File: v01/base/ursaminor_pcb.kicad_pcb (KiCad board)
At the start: 2 copper layers, 298.8 x 122 mm, 143 parts, among them J1 USB_C_Receptacle_USB2.0, J2 I2C-L, J3 I2C-R, J4 AVR-ISP-6, SW1 Reset, U1 ATmega32U4-AU, U2 MCP23017_SO, U3 PRTR5V0U2X, U4 HOLE, Y1 16Mhz

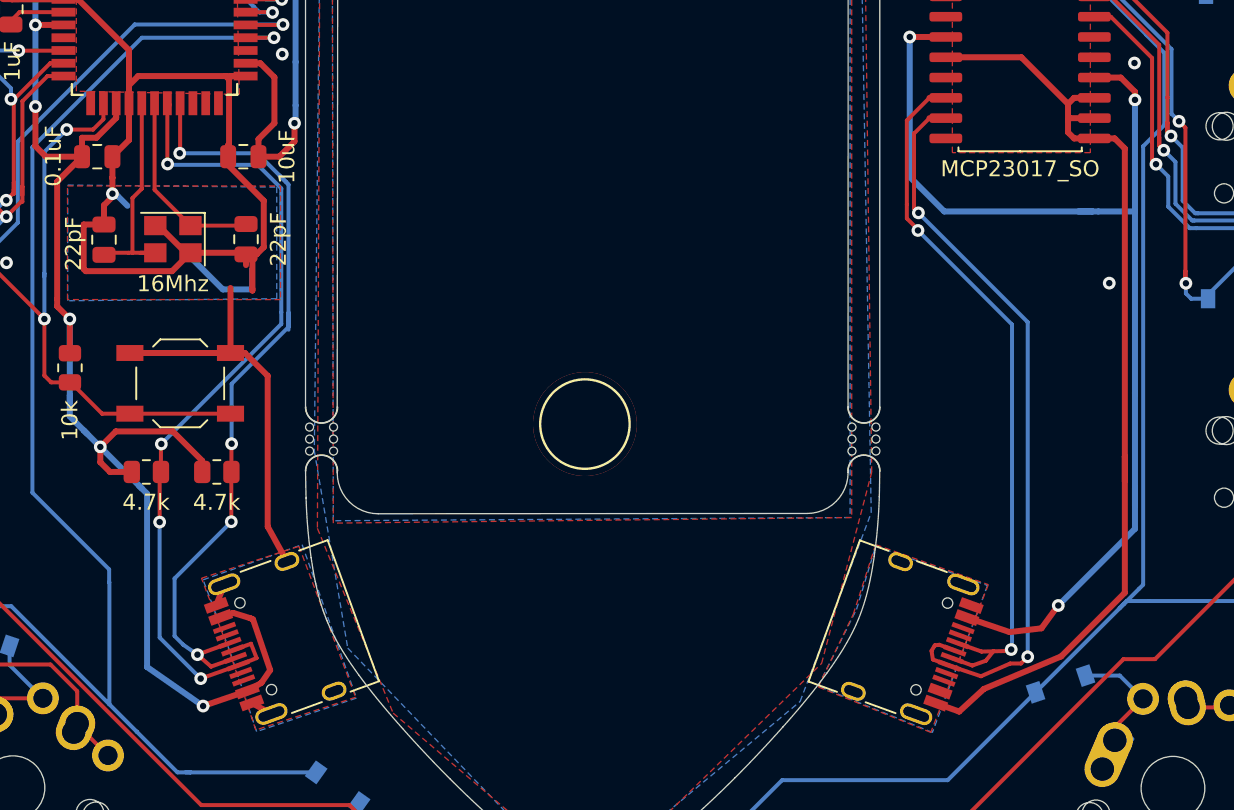
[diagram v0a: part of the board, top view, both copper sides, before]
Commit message: Rename files and update path references.
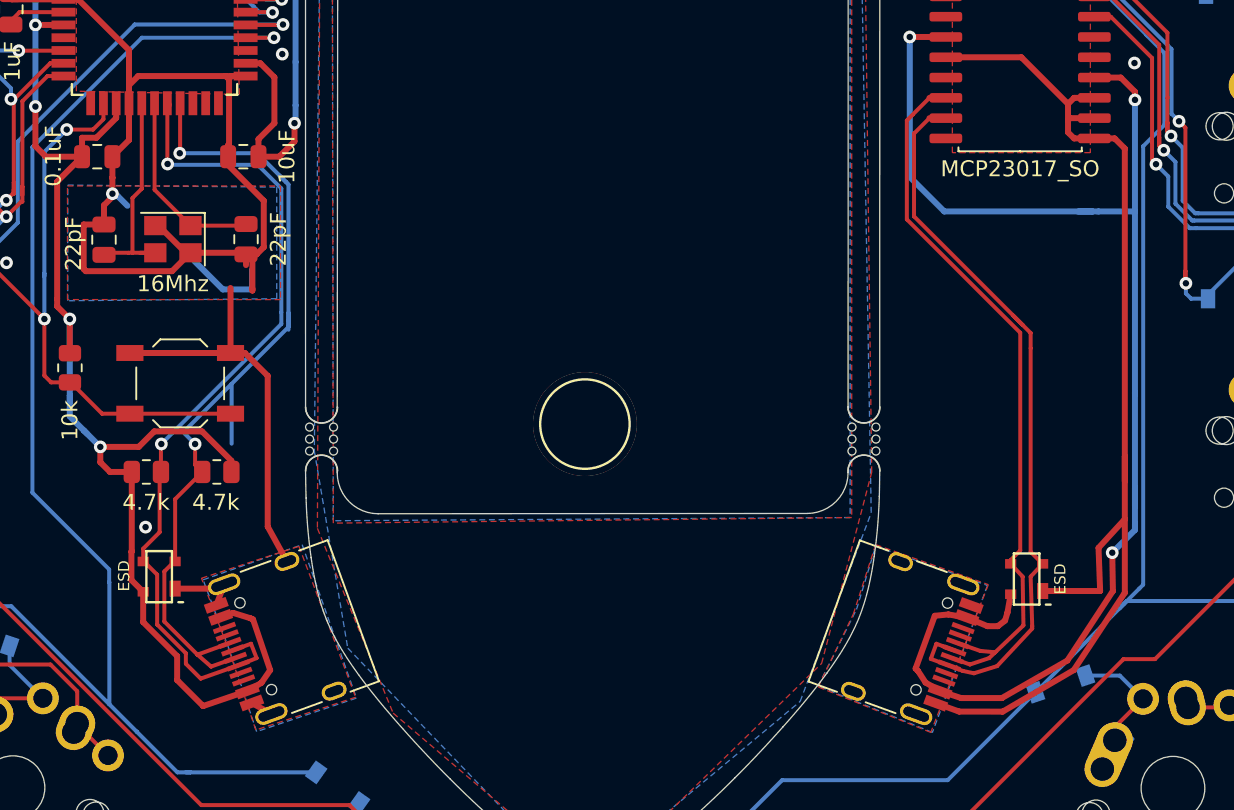
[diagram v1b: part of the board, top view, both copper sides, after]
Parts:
- added U4: PRTR5V0U2X, Keebio-Parts:SOT-143B, F.Cu at (148.8, 111.2)
- added U5: PRTR5V0U2X, Keebio-Parts:SOT-143B, F.Cu at (203.2, 111.4)
- turned R7 to 180 degrees
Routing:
- net VBUS: track 71.8 -> 89.1 mm
- net VSS: track 61.9 -> 71.4 mm, vias 4 -> 3
- net SDA-L: track 50.4 -> 55.6 mm, vias 4 -> 2
- net GND: track 194.2 -> 197.4 mm, vias 13 -> 14
- net SDA-R: track 46.8 -> 48.4 mm, vias 2 -> 0
- net +5V: track 207.6 -> 206.4 mm, vias 9 -> 8
- net SCL-R: track 45.4 -> 46.0 mm, vias 2 -> 0
- net SCL-L: track 53.1 -> 53.7 mm, vias 4 -> 2
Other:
- board text added: "Ursa Minor rev01 : markstory"
- board text removed: "Tryptris rev01 : markstory"

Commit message: Fix DRC and add jcl tag
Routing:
- net VSS: track 71.4 -> 74.5 mm
- net Col5: track 141.3 -> 142.4 mm
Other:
- board text added: "JLCJLCJLCJLC"

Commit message: Remove silkscreen from contacts and pad.
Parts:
- moved G*** 0.80 mm to (100.6, 87.7)
- moved G*** 0.10 mm to (251.4, 88.1)
